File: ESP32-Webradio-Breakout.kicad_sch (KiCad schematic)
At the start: 50 parts, among them J1 AudioJack3, J2 Conn_01x01, J3 Micro_SD_Card, J4 Conn_01x02, P1 USB_C_Plug, Q1 BC817, Q2 BC817, Q3 BC817, SW1 RotaryEncoder_Switch, U1 AMS1117-3.3, U2 ESP32-WROOM-32, U3 CH340C, U4 PCF8574TS, U5 DS18B20

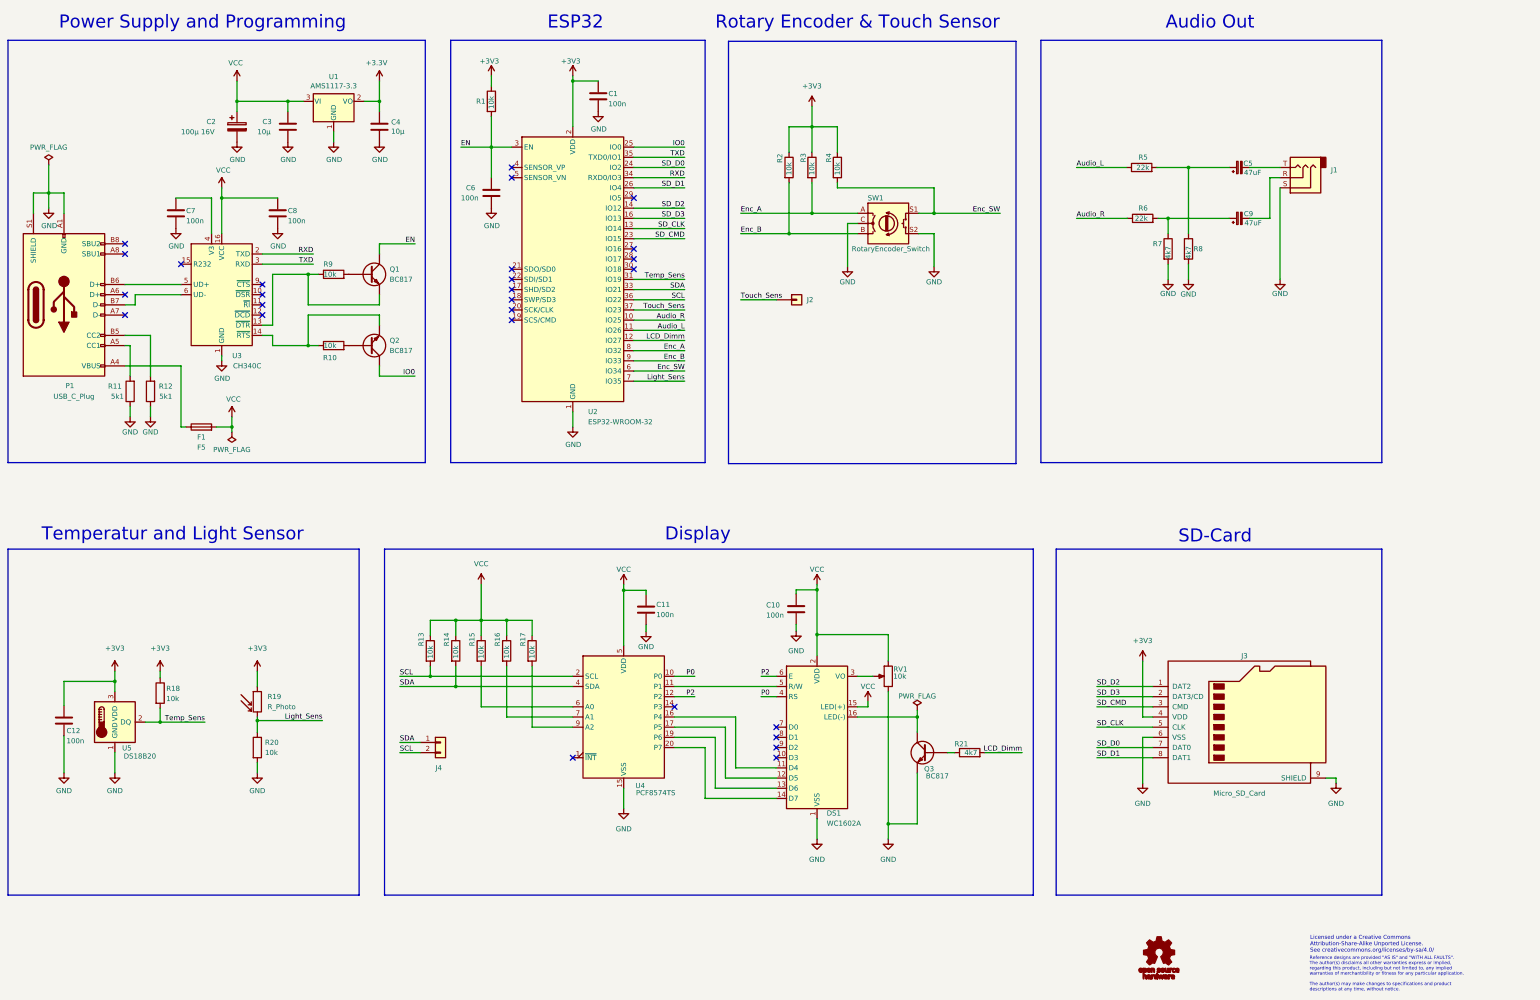
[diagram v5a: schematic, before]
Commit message: Added MicroSD slot Changed footprints for I2C, temp_sens, light_sens and rotary encoder to solder pads New parts placement
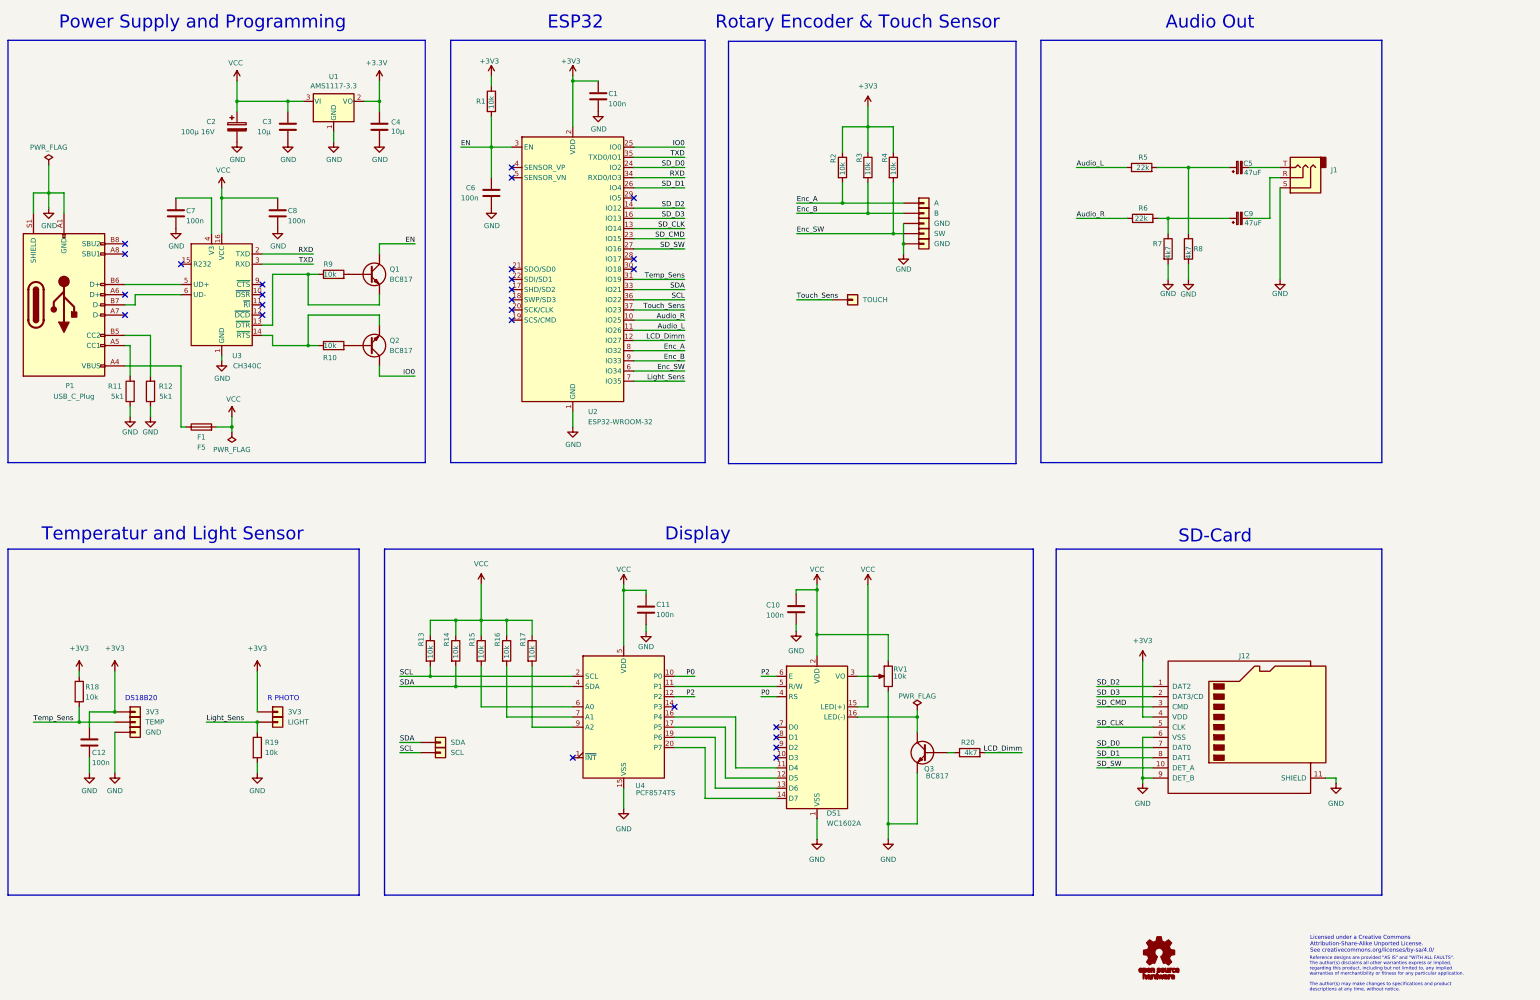
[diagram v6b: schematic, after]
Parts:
- removed J3: Micro_SD_Card, Connector_Card:microSD_HC_Wuerth_693072010801, symbol Connector:Micro_SD_Card
- removed J4: Conn_01x02, Connector_PinHeader_2.54mm:PinHeader_1x02_P2.54mm_Vertical, symbol Connector_Generic:Conn_01x02
- removed R19: R_Photo, OptoDevice:R_LDR_5.1x4.3mm_P3.4mm_Vertical, symbol Device:R_Photo
- removed SW1: RotaryEncoder_Switch, Rotary_Encoder:RotaryEncoder_Alps_EC11E-Switch_Vertical_H20mm, symbol Device:RotaryEncoder_Switch
- removed U5: DS18B20, Connector_PinHeader_2.54mm:PinHeader_1x03_P2.54mm_Vertical, symbol Sensor_Temperature:DS18B20
- added J10: TEMP, TestPoint:TestPoint_Pad_2.0x2.0mm, symbol Connector_Generic:Conn_01x01
- added J11: LIGHT, TestPoint:TestPoint_Pad_2.0x2.0mm, symbol Connector_Generic:Conn_01x01
- added J12: Micro_SD_Card_Det, Connector_Card:microSD_HC_Molex_104031-0811, symbol Connector:Micro_SD_Card_Det
- added J13, J4, J6: GND, TestPoint:TestPoint_Pad_2.0x2.0mm, symbol Connector_Generic:Conn_01x01
- added J14: SDA, TestPoint:TestPoint_Pad_2.0x2.0mm, symbol Connector_Generic:Conn_01x01
- added J15: SCL, TestPoint:TestPoint_Pad_2.0x2.0mm, symbol Connector_Generic:Conn_01x01
- added J2: A, TestPoint:TestPoint_Pad_2.0x2.0mm, symbol Connector_Generic:Conn_01x01
- added J3: B, TestPoint:TestPoint_Pad_2.0x2.0mm, symbol Connector_Generic:Conn_01x01
- added J5: SW, TestPoint:TestPoint_Pad_2.0x2.0mm, symbol Connector_Generic:Conn_01x01
- added J8, J9: 3V3, TestPoint:TestPoint_Pad_2.0x2.0mm, symbol Connector_Generic:Conn_01x01
- J7: renamed from J2; value Conn_01x01 -> TOUCH; footprint Connector_PinHeader_2.54mm:PinHeader_1x01_P2.54mm_Vertical -> TestPoint:TestPoint_Pad_2.0x2.0mm
- renumbered R20 to R19, R21 to R20
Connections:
- net +3V3: now also J12.4 (VDD), J8.1 (Pin_1), J9.1 (Pin_1)
- net Enc_A: now also R2.2, J2.1 (Pin_1); no longer R3.2
- net Enc_B: now also R3.2, J3.1 (Pin_1); no longer R2.2
- net Enc_SW: now also J5.1 (Pin_1)
- net GND: now also J12.11 (SHIELD), J12.6 (VSS), J12.9 (DET_B), J13.1 (Pin_1), J4.1 (Pin_1), J6.1 (Pin_1)
- net Light_Sens: now also J11.1 (Pin_1)
- net SCL: now also J15.1 (Pin_1)
- net SDA: now also J14.1 (Pin_1)
- net SD_CLK: now also J12.5 (CLK)
- net SD_CMD: now also J12.3 (CMD)
- net SD_D0: now also J12.7 (DAT0)
- net SD_D1: now also J12.8 (DAT1)
- net SD_D2: now also J12.1 (DAT2)
- net SD_D3: now also J12.2 (DAT3/CD)
- net Temp_Sens: now also J10.1 (Pin_1)
- net SD_SW: now reaches U2.27 (IO16)
- net SD_SW: now also J12.10 (DET_A)
- no-connect marks 27 -> 26
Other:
- note added: "DS18B20"
- note added: "R PHOTO"
- moved on the sheet: C12, R18, R2, R3, R4
